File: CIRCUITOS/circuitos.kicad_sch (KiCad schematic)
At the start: 10 parts, among them U1 LM358, U2 LM358, U3 LM35-D, U4 LM358

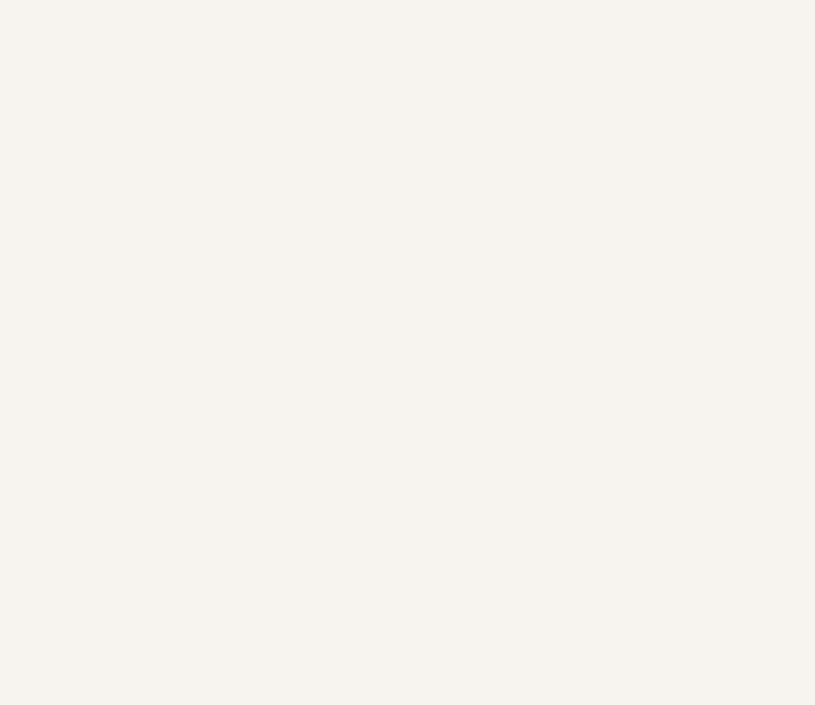
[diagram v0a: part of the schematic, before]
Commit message: Cambie el nombre monitoreo térmico a CIRCUITOS y estoy trabajando en unificar lo que ya hicimos
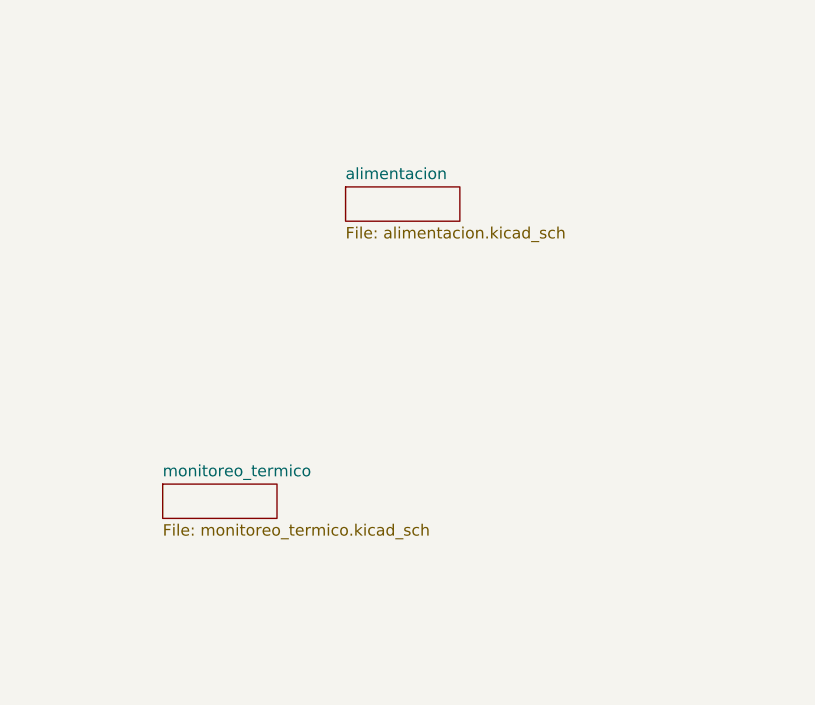
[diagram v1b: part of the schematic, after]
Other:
- added sheet alimentacion (alimentacion.kicad_sch)
- added sheet monitoreo_termico (monitoreo_termico.kicad_sch)
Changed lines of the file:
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@@
 		)
 		(instances
-			(project "monitoreo_termico"
+			(project "circuitos"
 				(path "/a0aa5472-87de-4e10-861a-104b546c9985"
 					(page "2")
 				)
 			)
+		)
+	)
+	(sheet
+		(at 217.17 59.69)
+		(size 12.7 3.81)
+		(exclude_from_sim no)
+		(in_bom yes)
+		(on_board yes)
+		(dnp no)
+		(fields_autoplaced yes)
+		(stroke
+			(width 0.1524)
+			(type solid)
+		)
+		(fill
+			(color 0 0 0 0.0000)
+		)
+		(property "Sheetname" "alimentacion"
+			(at 217.17 58.9784 0)
+			(effects
+				(font
+					(size 1.27 1.27)
+				)
+				(justify left bottom)
+			)
+		)
+		(property "Sheetfile" "alimentacion.kicad_sch"
+			(at 217.17 64.0846 0)
+			(effects
+				(font
+					(size 1.27 1.27)
+				)
+				(justify left top)
+			)
+		)
+		(instances
+			(project "circuitos"
+				(path "/a0aa5472-87de-4e10-861a-104b546c9985"
+					(page "3")
+				)
+			)
+		)
+	)
+	(sheet
+		(at 196.85 92.71)
+		(size 12.7 3.81)
+		(exclude_from_sim no)
+		(in_bom yes)
+		(on_board yes)
+		(dnp no)
+		(fields_autoplaced yes)
+		(stroke
+			(width 0.1524)
+			(type solid)
+		)
+		(fill
+			(color 0 0 0 0.0000)
+		)
+		(property "Sheetname" "monitoreo_termico"
+			(at 196.85 91.9984 0)
+			(effects
+				(font
+					(size 1.27 1.27)
+				)
+				(justify left bottom)
+			)
+		)
+		(property "Sheetfile" "monitoreo_termico.kicad_sch"
+			(at 196.85 97.1046 0)
+			(effects
+				(font
+					(size 1.27 1.27)
+				)
+				(justify left top)
+			)
+		)
+		(instances
+			(project "circuitos"
+				(path "/a0aa5472-87de-4e10-861a-104b546c9985"
+					(page "4")
+				)
+			)

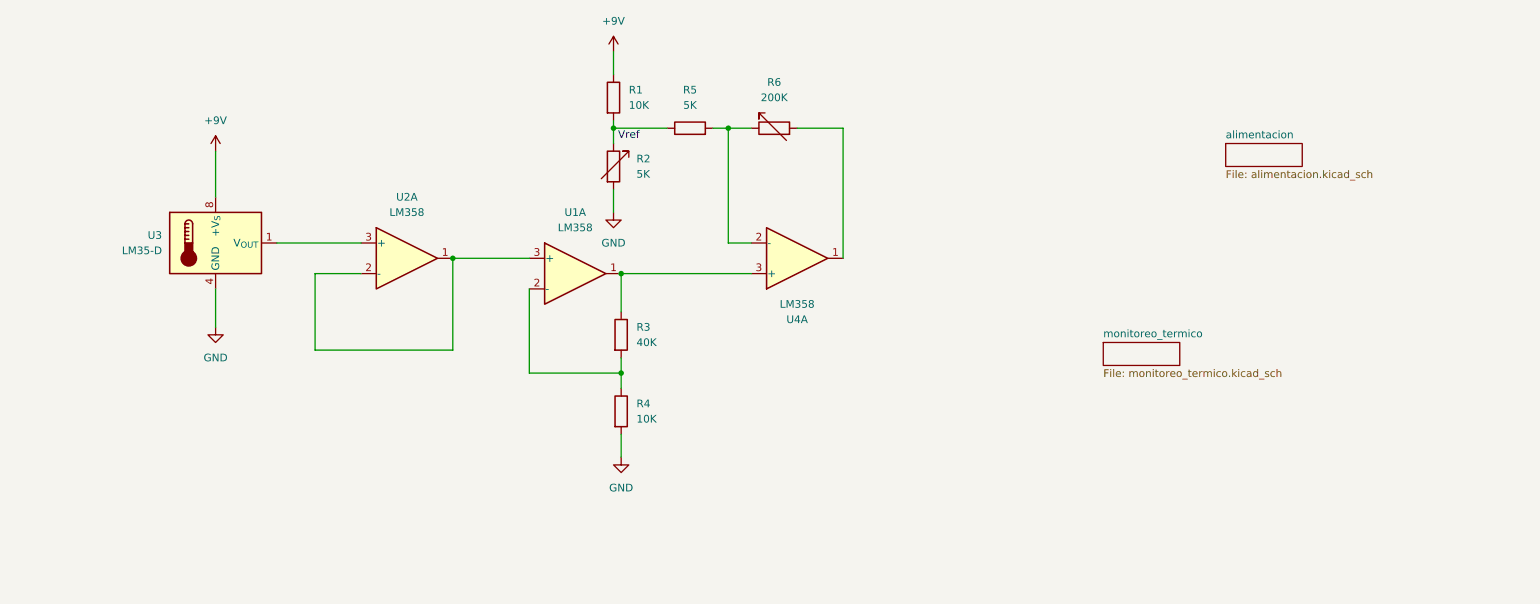
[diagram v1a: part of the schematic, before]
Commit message: Agregue TP11
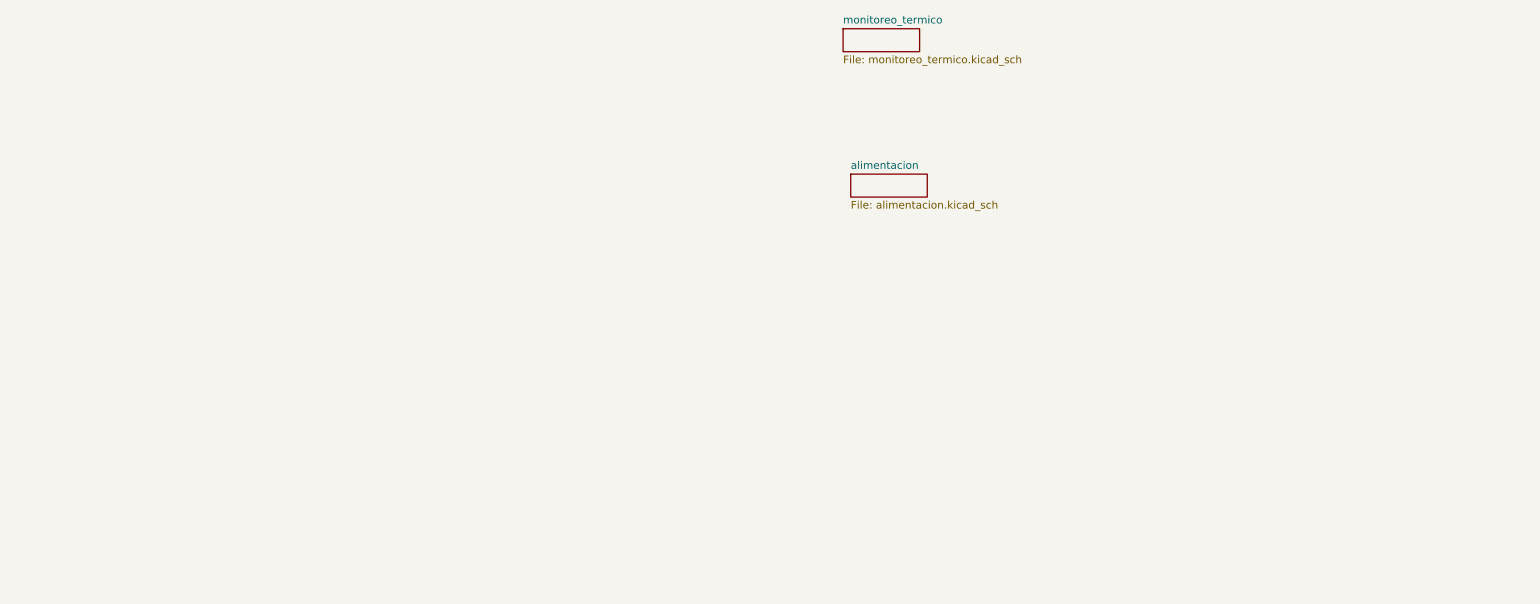
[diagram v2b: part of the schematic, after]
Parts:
- removed R1, R4: 10K, symbol Device:R
- removed R2: 5K, symbol Device:R_Variable
- removed R3: 40K, symbol Device:R
- removed R5: 5K, symbol Device:R
- removed R6: 200K, symbol Device:R_Variable
- removed U1, U2, U4: LM358, symbol Amplifier_Operational:LM358
- removed U3: LM35-D, Package_SO:SOIC-8_3.9x4.9mm_P1.27mm, symbol Sensor_Temperature:LM35-D
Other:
- note removed: "Vref"
